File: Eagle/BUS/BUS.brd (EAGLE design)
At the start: 100 x 120 mm, 14 parts

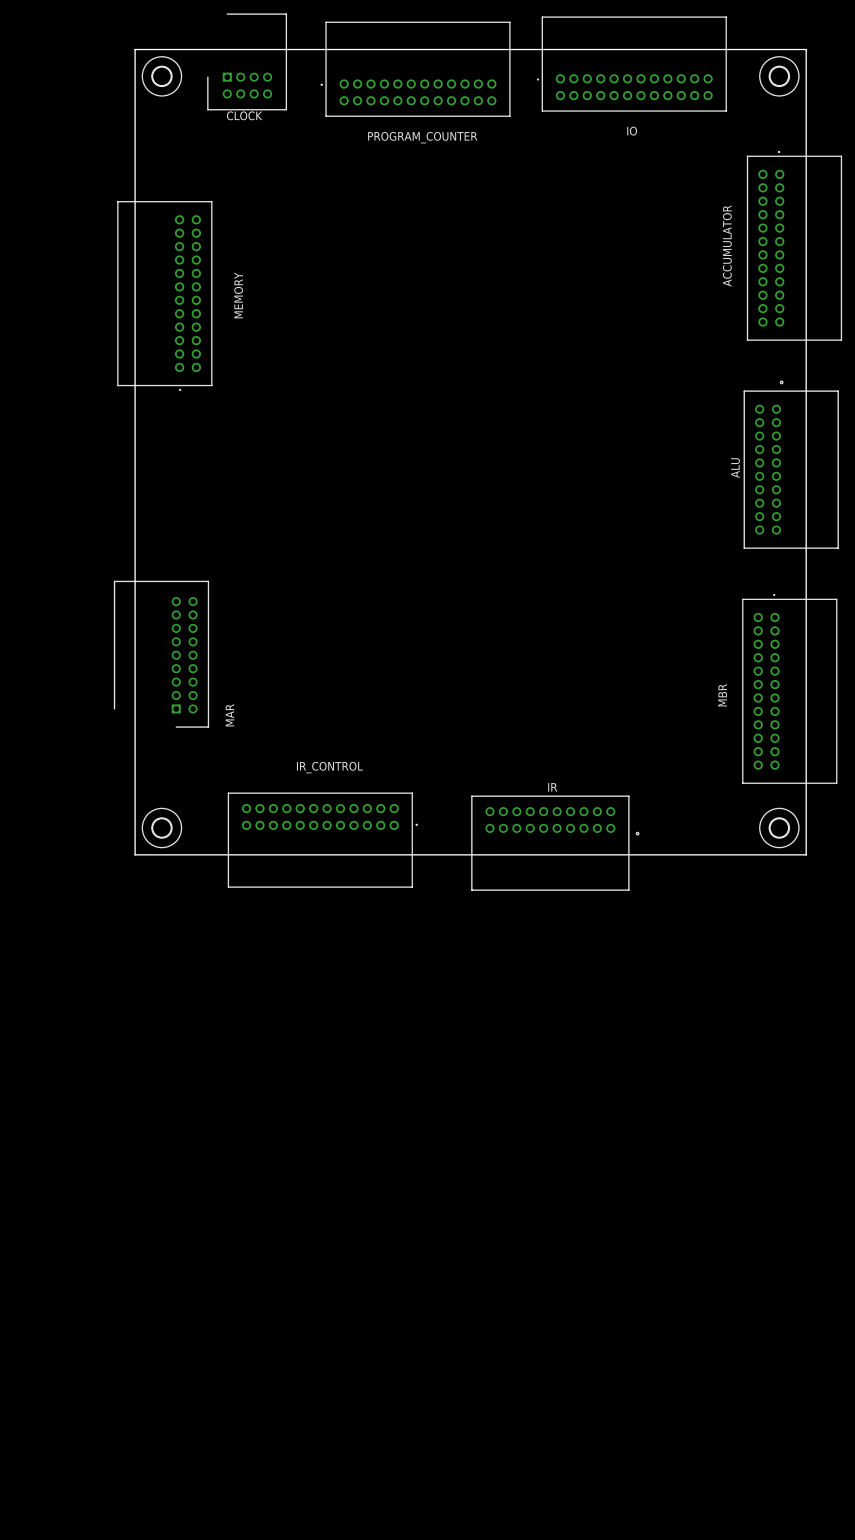
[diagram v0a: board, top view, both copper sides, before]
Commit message: added BUS
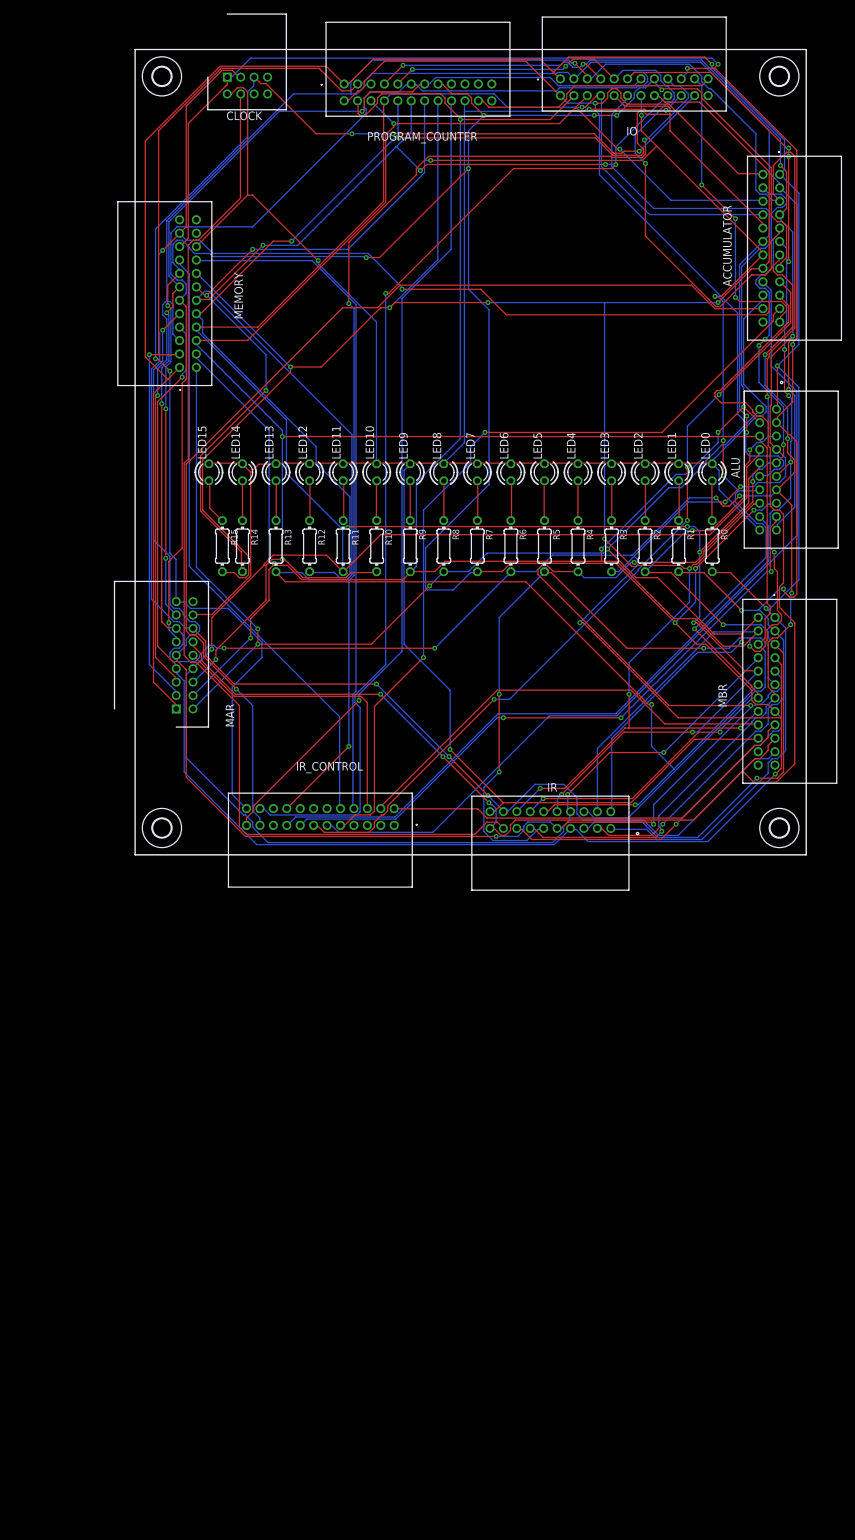
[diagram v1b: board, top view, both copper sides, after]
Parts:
- added LED0, LED1, LED10, LED11, LED12, LED13, LED14, LED15, LED2, LED3, LED4, LED5, LED6, LED7, LED8, LED9: RED, led:LED3MM
- added R0, R1, R10, R11, R12, R13, R14, R15, R2, R3, R4, R5, R6, R7, R8, R9: 220, rcl:0204/7
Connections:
- new net !CLK: CLOCK.4, IR.17
- new net ACI: ACCUMULATOR.17, IR_CONTROL.13
- new net ACO: ACCUMULATOR.18, IR_CONTROL.11
- new net ALUO: ALU.17, IR_CONTROL.15
- new net B0: ACCUMULATOR.1, ALU.1, IO.1, IR.1, MAR.1, MBR.1, MEMORY.1, PROGRAM_COUNTER.1, R0.2
- new net B1: ACCUMULATOR.3, ALU.3, IO.3, IR.3, MAR.3, MBR.3, MEMORY.3, PROGRAM_COUNTER.3, R1.2
- new net B10: ACCUMULATOR.6, ALU.6, IO.6, IR.6, MAR.6, MBR.6, MEMORY.6, PROGRAM_COUNTER.6, R10.2
- new net B11: ACCUMULATOR.8, ALU.8, IO.8, IR.8, MAR.8, MBR.8, MEMORY.8, PROGRAM_COUNTER.8, R11.2
- new net B12: ACCUMULATOR.10, ALU.10, IO.10, IR.10, MBR.10, MEMORY.10, PROGRAM_COUNTER.10, R12.2
- new net B13: ACCUMULATOR.12, ALU.12, IO.12, IR.12, MBR.12, MEMORY.12, PROGRAM_COUNTER.12, R13.2
- new net B14: ACCUMULATOR.14, ALU.14, IO.14, IR.14, MBR.14, MEMORY.14, PROGRAM_COUNTER.14, R14.2
- new net B15: ACCUMULATOR.16, ALU.16, IO.16, IR.16, MBR.16, MEMORY.16, PROGRAM_COUNTER.16, R15.2
- new net B2: ACCUMULATOR.5, ALU.5, IO.5, IR.5, MAR.5, MBR.5, MEMORY.5, PROGRAM_COUNTER.5, R2.2
- new net B3: ACCUMULATOR.7, ALU.7, IO.7, IR.7, MAR.7, MBR.7, MEMORY.7, PROGRAM_COUNTER.7, R3.2
- new net B4: ACCUMULATOR.9, ALU.9, IO.9, IR.9, MAR.9, MBR.9, MEMORY.9, PROGRAM_COUNTER.9, R4.2
- new net B5: ACCUMULATOR.11, ALU.11, IO.11, IR.11, MAR.11, MBR.11, MEMORY.11, PROGRAM_COUNTER.11, R5.2
- new net B6: ACCUMULATOR.13, ALU.13, IO.13, IR.13, MAR.13, MBR.13, MEMORY.13, PROGRAM_COUNTER.13, R6.2
- new net B7: ACCUMULATOR.15, ALU.15, IO.15, IR.15, MAR.15, MBR.15, MEMORY.15, PROGRAM_COUNTER.15, R7.2
- new net B8: ACCUMULATOR.2, ALU.2, IO.2, IR.2, MAR.2, MBR.2, MEMORY.2, PROGRAM_COUNTER.2, R8.2
- new net B9: ACCUMULATOR.4, ALU.4, IO.4, IR.4, MAR.4, MBR.4, MEMORY.4, PROGRAM_COUNTER.4, R9.2
- new net C0: IR_CONTROL.1
- new net C1: IR_CONTROL.3
- new net C2: IR_CONTROL.5
- new net C3: IR_CONTROL.7
- new net CE: ACCUMULATOR.22, IR_CONTROL.21
- new net CLK: ACCUMULATOR.23, CLOCK.3, IO.21, IR.18, MAR.14, MBR.21, MEMORY.21
- new net CO: IR_CONTROL.19
- new net GND: ACCUMULATOR.20, ALU.20, CLOCK.2, IO.20, IR.20, LED0.K, LED1.K, LED10.K, LED11.K, LED12.K, LED13.K, LED14.K, LED15.K, LED2.K, LED3.K, LED4.K, LED5.K, LED6.K, LED7.K, LED8.K, LED9.K, MAR.16, MBR.20, MEMORY.20, PROGRAM_COUNTER.20
- new net HLT: CLOCK.5, IO.22, IR_CONTROL.24, MAR.17
- new net INPUT: IO.17, IR_CONTROL.18
- new net IRI: IR_CONTROL.16
- new net IRO: IR_CONTROL.14
- new net JMP: IR_CONTROL.23, PROGRAM_COUNTER.18
- new net MARI: IR_CONTROL.6, MAR.10
- new net MBRI: IR_CONTROL.2, MBR.17
- new net MBRO: IR_CONTROL.4, MBR.18
- new net MCR: IR_CONTROL.20
- new net N$1: LED1.A, R1.1
- new net N$10: PROGRAM_COUNTER.19
- new net N$11: PROGRAM_COUNTER.21
- new net N$12: PROGRAM_COUNTER.23
- new net N$13: LED9.A, R9.1
- new net N$14: LED10.A, R10.1
- new net N$15: LED11.A, R11.1
- new net N$16: LED12.A, R12.1
- new net N$17: LED13.A, R13.1
- new net N$18: LED14.A, R14.1
- new net N$19: LED15.A, R15.1
- new net N$2: LED2.A, R2.1
- new net N$20: LED0.A, R0.1
- new net N$3: LED3.A, R3.1
- new net N$4: LED4.A, R4.1
- new net N$5: LED5.A, R5.1
- new net N$6: LED6.A, R6.1
- new net N$7: LED7.A, R7.1
- new net N$8: LED8.A, R8.1
- new net N$9: PROGRAM_COUNTER.17
- new net OI: IO.18, IR_CONTROL.22
- new net ONE: IR_CONTROL.12
- new net RI: IR_CONTROL.8, MEMORY.18
- new net RO: IR_CONTROL.10, MEMORY.17
- new net RST: IO.23, PROGRAM_COUNTER.22
- new net SC: ACCUMULATOR.21, IR_CONTROL.9
- new net SU: ALU.18, IR_CONTROL.17
- new net SWITCHVCC: ACCUMULATOR.19, IR.19, MAR.12, MBR.19
- new net VCC: ALU.19, CLOCK.1, IO.19, MEMORY.19
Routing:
- net GND: track 0.00 -> 417.0 mm, vias 0 -> 4
- net B4: track 0.00 -> 415.3 mm, vias 0 -> 12
- net B7: track 0.00 -> 402.5 mm, vias 0 -> 13
- net B11: track 0.00 -> 393.5 mm, vias 0 -> 4
- net B3: track 0.00 -> 392.2 mm, vias 0 -> 9
- net B6: track 0.00 -> 378.8 mm, vias 0 -> 12
- net B5: track 0.00 -> 368.8 mm, vias 0 -> 12
- net B9: track 0.00 -> 367.1 mm, vias 0 -> 6
- net B2: track 0.00 -> 364.5 mm, vias 0 -> 7
- net B0: track 0.00 -> 350.4 mm, vias 0 -> 3
- net B13: track 0.00 -> 348.8 mm, vias 0 -> 7
- net B8: track 0.00 -> 346.4 mm, vias 0 -> 6
- net CLK: track 0.00 -> 346.2 mm, vias 0 -> 8
- net B15: track 0.00 -> 344.8 mm, vias 0 -> 9
- net B10: track 0.00 -> 342.1 mm, vias 0 -> 5
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
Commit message: added pull down resistors and reset circuit to BUS
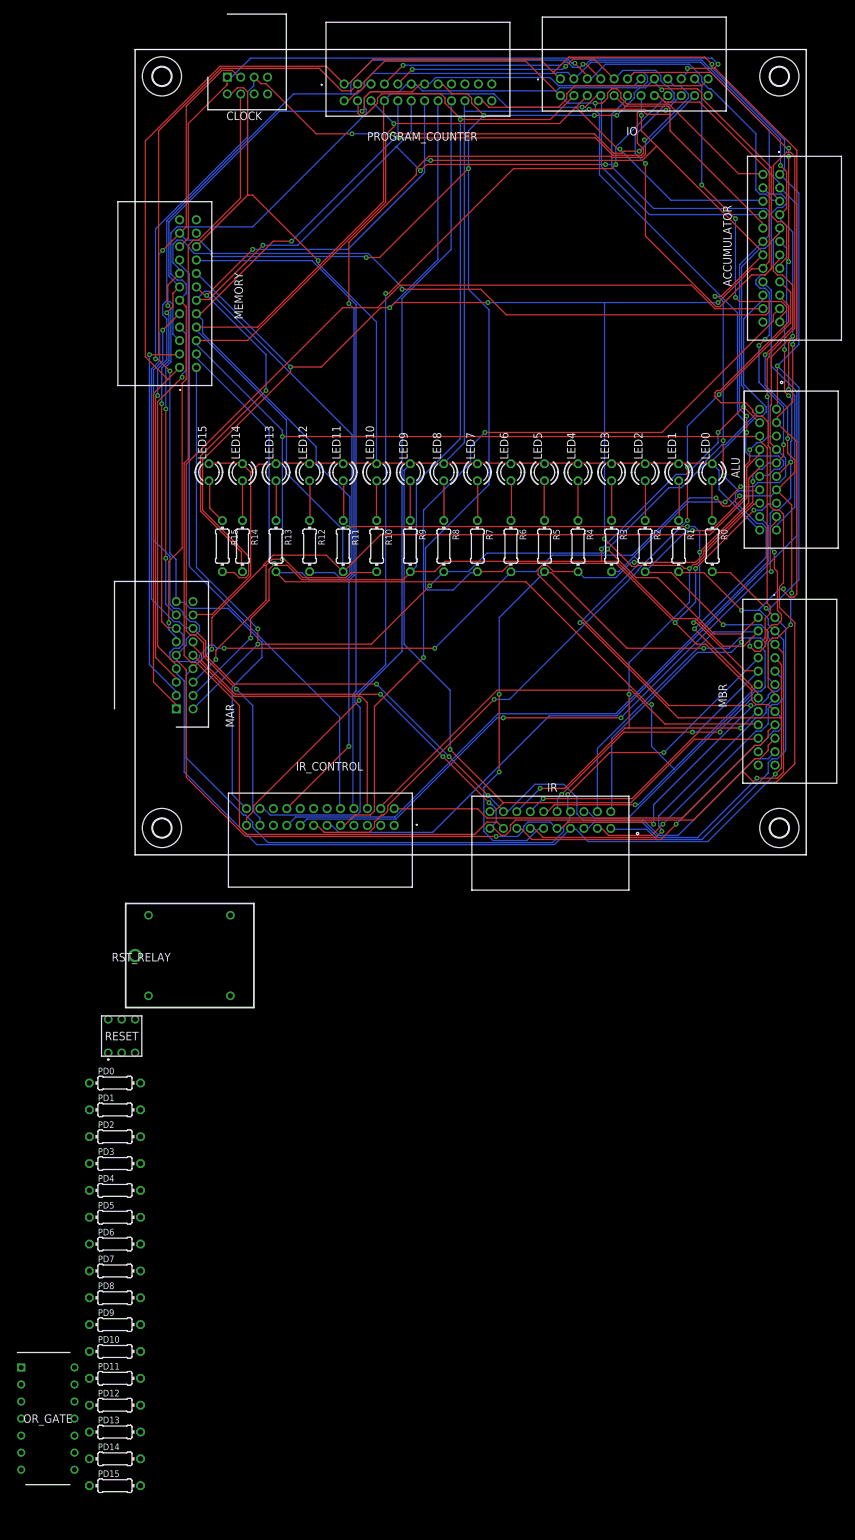
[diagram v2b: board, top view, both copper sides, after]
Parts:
- added OR_GATE: SN74HC32N, SamacSys_Parts:DIP794W53P254L1930H508Q14N
- added PD0, PD1, PD10, PD11, PD12, PD13, PD14, PD15, PD2, PD3, PD4, PD5, PD6, PD7, PD8, PD9: 10k, rcl:0204/7
- added RESET: MHPS2273N, SamacSys_Parts:MHPS2273N
- added RST_RELAY: SRD-05VDC-SL-C, SamacSys_Parts:SRD
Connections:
- removed net N$10: PROGRAM_COUNTER.19
- removed net N$12: PROGRAM_COUNTER.23
- removed net N$9: PROGRAM_COUNTER.17
- new net !RST: PROGRAM_COUNTER.22, RESET.A2
- new net AC_CE: ACCUMULATOR.22, OR_GATE.1
- new net CL_CE: IR_CONTROL.21, OR_GATE.2
- new net CL_HLT: IR_CONTROL.24, OR_GATE.5
- new net IO_HLT: IO.22, OR_GATE.10
- new net MAR_HLT: MAR.17, OR_GATE.4
- net B0: now also PD0.2
- net B1: now also PD1.2
- net B10: now also PD10.2
- net B11: now also PD11.2
- net B12: now also PD12.2
- net B13: now also PD13.2
- net B14: now also PD14.2
- net B15: now also PD15.2
- net B2: now also PD2.2
- net B3: now also PD3.2
- net B4: now also PD4.2
- net B5: now also PD5.2
- net B6: now also PD6.2
- net B7: now also PD7.2
- net B8: now also PD8.2
- net B9: now also PD9.2
- net CE: now also OR_GATE.3, PROGRAM_COUNTER.23; no longer ACCUMULATOR.22, IR_CONTROL.21
- net CLK: now also PROGRAM_COUNTER.21
- net CO: now also PROGRAM_COUNTER.17
- net GND: now also OR_GATE.12, OR_GATE.13, OR_GATE.7, PD0.1, PD1.1, PD10.1, PD11.1, PD12.1, PD13.1, PD14.1, PD15.1, PD2.1, PD3.1, PD4.1, PD5.1, PD6.1, PD7.1, PD8.1, PD9.1, RESET.A3, RST_RELAY.3
- net HLT: now also OR_GATE.8; no longer IO.22, IR_CONTROL.24, MAR.17
- net N$11: now also OR_GATE.6, OR_GATE.9; no longer PROGRAM_COUNTER.21
- net RST: now also RESET.B3, RST_RELAY.2; no longer PROGRAM_COUNTER.22
- net SWITCHVCC: now also RST_RELAY.1
- net VCC: now also OR_GATE.14, PROGRAM_COUNTER.19, RESET.A1, RESET.B2, RST_RELAY.5
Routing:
- net CE: track 157.3 -> 0.00 mm, vias 1 -> 0
- net CL_CE: track 0.00 -> 157.1 mm, vias 0 -> 1
- net HLT: track 202.4 -> 159.5 mm
- net CL_HLT: track 0.00 -> 42.6 mm

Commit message: added flyback diode
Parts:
- added FLYBACK_DIODE: 1N4148DO35-7, diode:DO35-7
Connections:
- net GND: now also FLYBACK_DIODE.A
- net RST: now also FLYBACK_DIODE.C
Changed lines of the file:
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@@
 <layer number="97" name="Info" color="7" fill="1" visible="no" active="no"/>
 <layer number="98" name="Guide" color="6" fill="1" visible="no" active="no"/>
+<layer number="99" name="SpiceOrder" color="5" fill="1" visible="no" active="no"/>
 </layers>
 <board>
@@
 <attribute name="VALUE" x="-13" y="-84" size="1.27" layer="27" align="center"/>
 </element>
+<element name="FLYBACK_DIODE" library="diode" library_urn="urn:adsk.eagle:library:210" package="DO35-7" package3d_urn="urn:adsk.eagle:package:43339/2" value="1N4148DO35-7" x="-13" y="-99" smashed="yes">
+<attribute name="NAME" x="-15.286" y="-97.73" size="1.27" layer="25" ratio="10"/>
+<attribute name="POPULARITY" value="58" x="-13" y="-99" size="1.778" layer="27" display="off"/>
+<attribute name="VALUE" x="-15.286" y="-101.667" size="1.27" layer="27" ratio="10"/>
+</element>
 </elements>
 <signals>
@@
 <contactref element="OR_GATE" pad="12"/>
 <contactref element="OR_GATE" pad="13"/>
+<contactref element="FLYBACK_DIODE" pad="A"/>
 <wire x1="-6.81" y1="-90" x2="-16.97" y2="-91.62" width="0" layer="19" extent="1-1"/>
 <wire x1="-6.81" y1="-94" x2="-6.81" y2="-90" width="0" layer="19" extent="1-1"/>
@@
 <wire x1="-6.81" y1="-38" x2="-6.81" y2="-42" width="0" layer="19" extent="1-1"/>
 <wire x1="-6.81" y1="-34" x2="-6.81" y2="-38" width="0" layer="19" extent="1-1"/>
+<wire x1="-9.19" y1="-99" x2="-6.81" y2="-94" width="0" layer="19" extent="1-1"/>
 <wire x1="0" y1="-29.5" x2="-6.81" y2="-34" width="0" layer="19" extent="1-1"/>
 <wire x1="2" y1="-21" x2="0" y2="-29.5" width="0" layer="19" extent="1-1"/>
@@
 <contactref element="RESET" pad="B3"/>
 <contactref element="RST_RELAY" pad="2"/>
+<contactref element="FLYBACK_DIODE" pad="C"/>
 <wire x1="2" y1="-9" x2="51.2064" y2="112.3188" width="0" layer="19" extent="1-1"/>
 <wire x1="0" y1="-24.5" x2="2" y2="-9" width="0" layer="19" extent="1-1"/>
+<wire x1="-16.81" y1="-99" x2="0" y2="-24.5" width="0" layer="19" extent="1-1"/>
 </signal>
 <signal name="N$1">

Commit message: added gerber files for each board
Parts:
- moved FLYBACK_DIODE 209.9 mm to (62.0, 97.0), turned to 270 degrees
- moved OR_GATE 180.9 mm to (29.0, 92.0), turned to 90 degrees
- moved RST_RELAY 129.7 mm to (67.0, 96.0)
- moved RESET 129.4 mm to (75.0, 77.0)
- moved PD15 126.9 mm to (19.0, 31.0), turned to 270 degrees
- moved PD14 123.8 mm to (23.0, 31.0), turned to 270 degrees
- moved PD13 120.8 mm to (27.0, 31.0), turned to 270 degrees
- moved PD12 118.0 mm to (31.0, 31.0), turned to 270 degrees
- moved PD11 115.4 mm to (35.0, 31.0), turned to 270 degrees
- moved PD10 113.1 mm to (39.0, 31.0), turned to 270 degrees
- moved PD9 111.0 mm to (43.0, 31.0), turned to 270 degrees
- moved PD8 109.1 mm to (47.0, 31.0), turned to 270 degrees
- moved PD7 107.5 mm to (51.0, 31.0), turned to 270 degrees
- moved PD6 106.2 mm to (55.0, 31.0), turned to 270 degrees
- moved PD5 105.2 mm to (59.0, 31.0), turned to 270 degrees
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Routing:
- net CO: track 0.00 -> 146.6 mm, vias 0 -> 1
- net HLT: track 159.5 -> 30.1 mm, vias 5 -> 0
- net GND: track 417.0 -> 510.4 mm, vias 4 -> 2
- net AC_CE: track 0.00 -> 82.4 mm
- net IO_HLT: track 0.00 -> 77.0 mm, vias 0 -> 1
- net MAR_HLT: track 0.00 -> 63.2 mm
- net CL_CE: track 157.1 -> 95.4 mm, vias 1 -> 0
- net B0: track 350.4 -> 406.3 mm, vias 3 -> 6
- net B6: track 378.8 -> 434.5 mm, vias 12 -> 10
- net B7: track 402.5 -> 457.1 mm, vias 13 -> 5
- net !RST: track 0.00 -> 51.6 mm
- net CL_HLT: track 42.6 -> 90.1 mm, vias 0 -> 2
- net SWITCHVCC: track 202.8 -> 246.2 mm
- net B10: track 342.1 -> 384.0 mm, vias 5 -> 12
- net B9: track 367.1 -> 408.4 mm, vias 6 -> 2
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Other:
- board text added: "MARIE PC BUS Architecture design by: Dr. Linda Null Hardware implementation by: Richard Bowser"

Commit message: added power connector
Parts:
- added POWER: 207479-0002, SamacSys_Parts:2074790002
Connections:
- net GND: now also POWER.2
- net VCC: now also POWER.1
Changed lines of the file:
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@@
 <drawing>
 <settings>
-<setting alwaysvectorfont="yes"/>
+<setting alwaysvectorfont="no"/>
 <setting verticaltext="up"/>
 </settings>
@@
 <attribute name="VALUE" x="59.333" y="99.286" size="1.27" layer="27" ratio="10" rot="R270"/>
 </element>
+<element name="POWER" library="SamacSys_Parts" package="2074790002" value="207479-0002" x="-9" y="1" smashed="yes">
+<attribute name="DESCRIPTION" value="MOLEX - 207479-0002 - L1NK 396 SHROUDED HEADER ASSEMBLY-1X2 98AC8497" x="-9" y="1" size="1.778" layer="27" display="off"/>
+<attribute name="HEIGHT" value="14.1mm" x="-9" y="1" size="1.778" layer="27" display="off"/>
+<attribute name="MANUFACTURER_NAME" value="Molex" x="-9" y="1" size="1.778" layer="27" display="off"/>
+<attribute name="MANUFACTURER_PART_NUMBER" value="207479-0002" x="-9" y="1" size="1.778" layer="27" display="off"/>
+<attribute name="MOUSER_PART_NUMBER" value="538-207479-0002" x="-9" y="1" size="1.778" layer="27" display="off"/>
+<attribute name="MOUSER_PRICE-STOCK" value="https://www.mouser.com/Search/Refine.aspx?Keyword=538-207479-0002" x="-9" y="1" size="1.778" layer="27" display="off"/>
+<attribute name="NAME" x="-10.98" y="1" size="1.27" layer="25" align="center"/>
+<attribute name="VALUE" x="-10.98" y="1" size="1.27" layer="27" align="center"/>
+</element>
 </elements>
 <signals>
@@
 <wire x1="72.9996" y1="74.5236" x2="73" y2="74.5" width="0.1524" layer="1"/>
 <via x="77.4192" y="98.1456" extent="1-16" drill="0.35"/>
+<contactref element="POWER" pad="1"/>
+<wire x1="-9" y1="1" x2="6.63" y2="90.63" width="0" layer="19" extent="1-1"/>
 </signal>
 <signal name="CLK">
@@
 <via x="19.6596" y="96.774" extent="1-16" drill="0.35"/>
 <via x="78.0288" y="17.8308" extent="1-16" drill="0.35"/>
+<contactref element="POWER" pad="2"/>
+<wire x1="-12.96" y1="1" x2="8.634" y2="35.742" width="0" layer="19" extent="1-1"/>
 </signal>
 <signal name="!CLK">

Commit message: added gerber files for ordering boards
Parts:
- moved POWER 102.4 mm to (8.00, 102.0), turned to 90 degrees
- moved MEMORY 10.0 mm to (5.63, 62.6)
- moved LED0 8.00 mm to (86.0, 49.0)
- moved LED1 8.00 mm to (81.0, 49.0)
- moved LED10 8.00 mm to (36.0, 49.0)
- moved LED11 8.00 mm to (31.0, 49.0)
- moved LED12 8.00 mm to (26.0, 49.0)
- moved LED13 8.00 mm to (21.0, 49.0)
- moved LED14 8.00 mm to (16.0, 49.0)
- moved LED15 8.00 mm to (11.0, 49.0)
- moved LED2 8.00 mm to (76.0, 49.0)
- moved LED3 8.00 mm to (71.0, 49.0)
- moved LED4 8.00 mm to (66.0, 49.0)
- moved LED5 8.00 mm to (61.0, 49.0)
- moved LED6 8.00 mm to (56.0, 49.0)
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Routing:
- net B1: track 339.9 -> 419.9 mm, vias 6 -> 3
- net B12: track 331.0 -> 408.6 mm, vias 5 -> 2
- net B8: track 369.8 -> 440.1 mm, vias 14 -> 5
- net B0: track 406.3 -> 350.9 mm, vias 6 -> 4
- net B9: track 408.4 -> 357.5 mm, vias 2 -> 8
- net B7: track 457.1 -> 418.0 mm
- net GND: track 510.4 -> 478.1 mm, vias 2 -> 0
- net B6: track 434.5 -> 405.6 mm, vias 10 -> 11
- net JMP: track 132.2 -> 160.6 mm, vias 3 -> 0
- net B2: track 400.4 -> 375.2 mm, vias 8 -> 6
- net VCC: track 222.2 -> 246.6 mm, vias 1 -> 4
- net B11: track 394.5 -> 418.8 mm, vias 9 -> 4
- net CLK: track 335.9 -> 359.5 mm, vias 11 -> 8
- net CO: track 146.6 -> 125.5 mm, vias 1 -> 4
- net B14: track 333.1 -> 353.2 mm, vias 12 -> 11
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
